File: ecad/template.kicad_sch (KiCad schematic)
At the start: 3 parts, among them P1 CF_EXP_LEFT, P2 CF_EXP_RIGHT

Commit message: Footprints working
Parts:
- removed B1: bitcraze_200, symbol template-rescue:bitcraze_200
- removed P1: CF_EXP_LEFT, symbol template-rescue:CF_EXP_LEFT
- removed P2: CF_EXP_RIGHT, symbol template-rescue:CF_EXP_RIGHT
- added J1, J2, J3, J4, J5, J6: Conn_01x03, Connector_PinHeader_2.54mm:PinHeader_1x03_P2.54mm_Horizontal, symbol Connector_Generic:Conn_01x03
- added J7, J8: Conn_01x01, Crazyflie:Servo_Power_GND_2.0x1.5mm, symbol Connector_Generic:Conn_01x01
- added J9: Conn_02x10_Counter_Clockwise, Crazyflie:Crazyflie_DeckHeader_2x10_P2.00_Vertical, symbol Connector_Generic:Conn_02x10_Counter_Clockwise
- added R1: 500k, Resistor_SMD:R_0603_1608Metric_Pad0.98x0.95mm_HandSolder, symbol Device:R_US
- added R2: 100k, Resistor_SMD:R_0603_1608Metric_Pad0.98x0.95mm_HandSolder, symbol Device:R_US
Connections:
- new net +BATT: J1.2 (Pin_2), J2.2 (Pin_2), J3.2 (Pin_2), J4.2 (Pin_2), J5.2 (Pin_2), J6.2 (Pin_2), J7.1 (Pin_1), R1.1
- new net GND: J1.3 (Pin_3), J2.3 (Pin_3), J3.3 (Pin_3), J4.3 (Pin_3), J5.3 (Pin_3), J6.3 (Pin_3), J8.1 (Pin_1), J9.10 (Pin_10), R2.2
- new net PWM1: J1.1 (Pin_1), J9.6 (Pin_6)
- new net PWM2: J2.1 (Pin_1), J9.7 (Pin_7)
- new net PWM3: J3.1 (Pin_1), J9.8 (Pin_8)
- new net PWM4: J4.1 (Pin_1), J9.19 (Pin_19)
- new net PWM5: J5.1 (Pin_1), J9.20 (Pin_20)
- new net PWM6: J6.1 (Pin_1), J9.16 (Pin_16)
- new net VBAT_MONITOR: J9.18 (Pin_18), R1.2, R2.1
- no-connect marks 0 -> 12

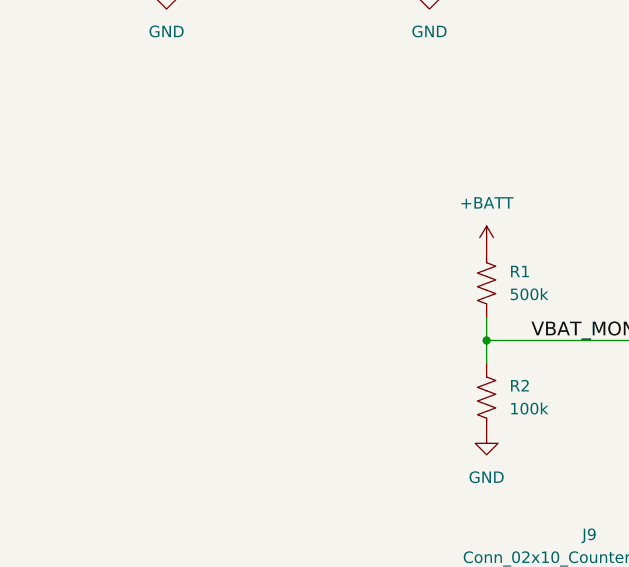
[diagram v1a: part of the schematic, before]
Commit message: Add power flags
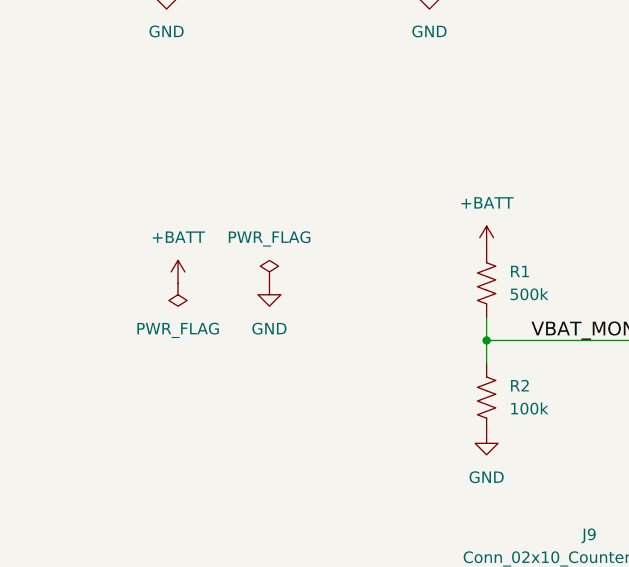
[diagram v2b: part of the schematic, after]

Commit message: Logan's changes
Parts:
- added C1, C2, C3, C4, C5, C6: 10u, Capacitor_SMD:C_0805_2012Metric_Pad1.18x1.45mm_HandSolder, symbol Device:C
- R1: value 500k -> 200k; footprint Resistor_SMD:R_0603_1608Metric_Pad0.98x0.95mm_HandSolder -> Resistor_SMD:R_0805_2012Metric_Pad1.20x1.40mm_HandSolder
- R2: footprint Resistor_SMD:R_0603_1608Metric_Pad0.98x0.95mm_HandSolder -> Resistor_SMD:R_0805_2012Metric_Pad1.20x1.40mm_HandSolder
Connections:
- net +BATT: now also C1.1, C2.1, C3.1, C4.1, C5.1, C6.1
- net GND: now also C1.2, C2.2, C3.2, C4.2, C5.2, C6.2
